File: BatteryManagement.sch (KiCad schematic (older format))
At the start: 21 parts, among them J201 Bootstrap, U201 AP9211, U202 MCP73213T-A6BI_MF, U203 BQ29209DRBR

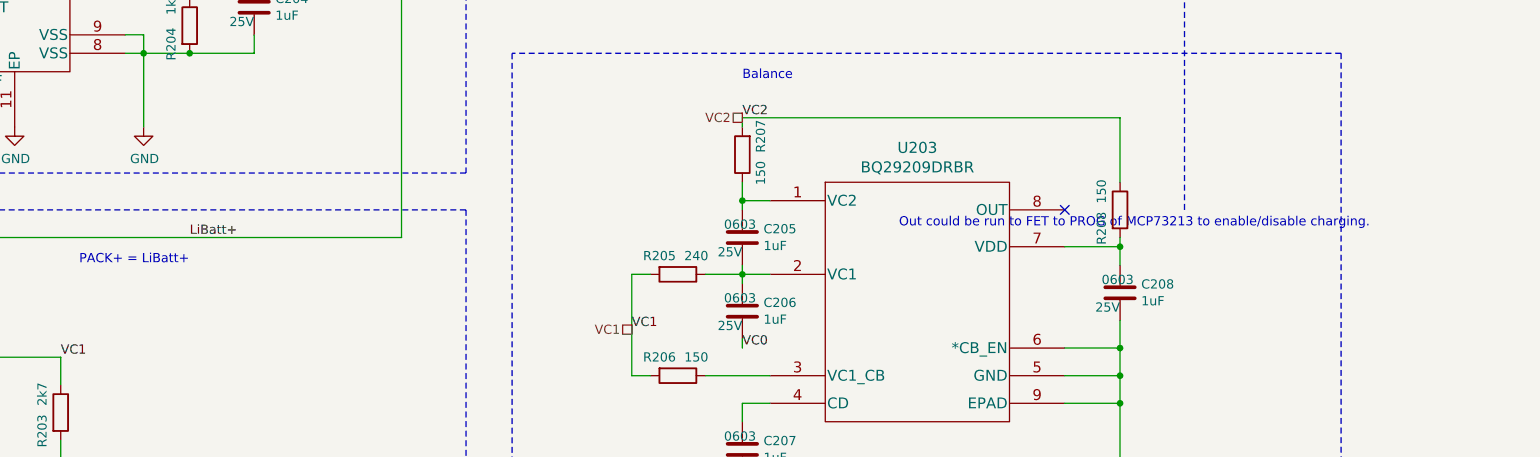
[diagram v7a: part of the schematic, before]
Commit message: Cleaning up the component links.
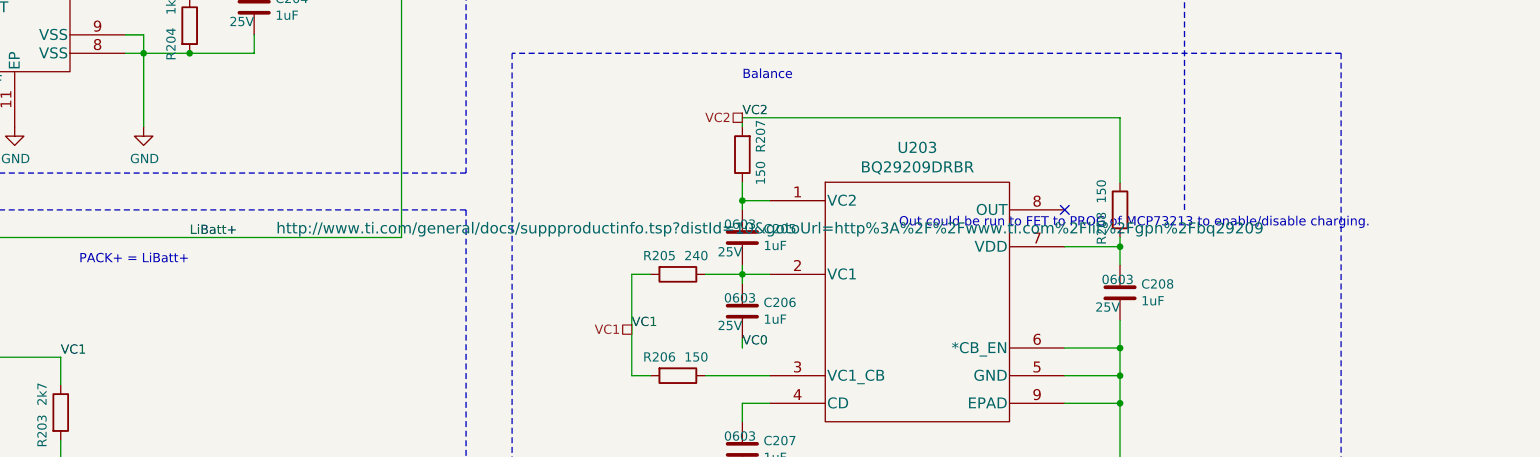
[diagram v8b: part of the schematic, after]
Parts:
- D201: footprint LED_SMD:LED_0603_1608Metric_Pad1.05x0.95mm_HandSolder -> LEDs:LED_0603
- R201: footprint Resistor_SMD:R_0603_1608Metric_Pad1.05x0.95mm_HandSolder -> Resistors_SMD:R_0603
- U203: footprint DRB8_1P6X2P4 -> libs:BQ29209DRBR; Link (none) -> https://www.digikey.com/product-detail/en/texas-instruments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; Mfg Part # (none) -> BQ29209DRBR; Package (none) -> 8-VDFN Exposed Pad; Supplier 1 (none) -> Digi-Key; Supplier Part Number 1 (none) -> 296-27677-1-ND; Unit Cost A$ (none) -> 0.90000
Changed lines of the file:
@@
 F 0 "R201" V 1700 4600 50  0000 C CNN
 F 1 "470" V 1700 4800 50  0000 C CNN
-F 2 "Resistor_SMD:R_0603_1608Metric_Pad1.05x0.95mm_HandSolder" V 1730 4700 50  0001 C CNN
+F 2 "Resistors_SMD:R_0603" V 1730 4700 50  0001 C CNN
 F 3 "~" H 1800 4700 50  0001 C CNN
 F 4 "0603" H 500 -1350 50  0001 C CNN "Package"
@@
 F 0 "D201" H 2142 2845 50  0000 C CNN
 F 1 "PWR" H 2142 2936 50  0000 C CNN
-F 2 "LED_SMD:LED_0603_1608Metric_Pad1.05x0.95mm_HandSolder" H 2150 3100 50  0001 C CNN
+F 2 "LEDs:LED_0603" H 2150 3100 50  0001 C CNN
 F 3 "~" H 2150 3100 50  0001 C CNN
 F 4 "0603" H 1250 -2950 50  0001 C CNN "Package"
@@
 F 0 "U203" H 8200 5537 60  0000 C CNN
 F 1 "BQ29209DRBR" H 8200 5431 60  0000 C CNN
-F 2 "DRB8_1P6X2P4" H 8200 4700 60  0001 C CNN
-F 3 "" H 7400 5100 60  0000 C CNN
+F 2 "libs:BQ29209DRBR" H 8200 4700 60  0001 C CNN
+F 3 "http://www.ti.com/general/docs/suppproductinfo.tsp?distId=10&gotoUrl=http%3A%2F%2Fwww.ti.com%2Flit%2Fgpn%2Fbq29209" H 7400 5100 60  0000 C CNN
+F 4 "https://www.digikey.com/product-detail/en/texas-instruments/BQ29209DRBR/296-27677-1-ND/2350211" H 8200 4700 50  0001 C CNN "Link"
+F 5 "BQ29209DRBR" H 8200 4700 50  0001 C CNN "Mfg Part #"
+F 6 "8-VDFN Exposed Pad" H 8200 4700 50  0001 C CNN "Package"
+F 7 "Digi-Key" H 8200 4700 50  0001 C CNN "Supplier 1"
+F 8 "296-27677-1-ND" H 8200 4700 50  0001 C CNN "Supplier Part Number 1"
+F 9 "0.90000" H 8200 4700 50  0001 C CNN "Unit Cost A$"
 	1    8200 4700
 	1    0    0    -1
